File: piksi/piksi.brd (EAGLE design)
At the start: 53 x 53 mm, 157 parts, among them J1 SMA_EDGE, J6 ZX62-B-5PA, Q1 IRLML6401, U1 6SLX9FTG256, U10 MAX2769, U12 PT7M8206B33TA5EX, U13 M25PX80, U2 LTC3407A_DFN, U3 STM32-M-64-LQFP, U4 7Q-16.368MBG-T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

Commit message: Fixed errors eagle 6.5 was complaining about
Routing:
- net SPI2MISO: track 53.6 -> 52.7 mm
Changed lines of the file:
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@@
 <?xml version="1.0" encoding="utf-8"?>
 <!DOCTYPE eagle SYSTEM "eagle.dtd">
-<eagle version="6.2">
+<eagle version="6.5.0">
 <drawing>
 <settings>
@@
 <wire x1="32.1564" y1="48.9204" x2="33.6804" y2="48.9204" width="0.2032" layer="113"/>
 <wire x1="30.861" y1="43.6626" x2="35.5854" y2="43.6626" width="0.2032" layer="113"/>
-<dimension x1="7.4" y1="7.4" x2="7.4" y2="52.4" x3="-0.2" y3="29.9" layer="48"/>
-<dimension x1="7.4" y1="52.4" x2="52.4" y2="52.4" x3="29.9" y3="59.8" layer="48"/>
-<dimension x1="7.9" y1="51.9" x2="4.38175" y2="54.70569375" x3="-1.71655" y3="59.568896875" layer="48" dtype="radius"/>
-<dimension x1="3.4" y1="7.9" x2="56.4" y2="7.9" x3="29.9" y3="-2.4" layer="48"/>
-<dimension x1="7.9" y1="56.4" x2="7.9" y2="3.4" x3="-8.1" y3="29.9" layer="48"/>
-<dimension x1="52.4" y1="7.4" x2="56.4" y2="7.4" x3="54.4" y3="-5.2" layer="48"/>
-<dimension x1="52.4" y1="7.4" x2="52.4" y2="3.4" x3="65.2" y3="5.4" layer="48"/>
-<dimension x1="52.4" y1="52.4" x2="58.8" y2="56.3" x3="61.2" y3="56.3" layer="48" dtype="leader"/>
+<dimension x1="7.4" y1="7.4" x2="7.4" y2="52.4" x3="-0.2" y3="29.9" textsize="3.5" layer="48"/>
+<dimension x1="7.4" y1="52.4" x2="52.4" y2="52.4" x3="29.9" y3="59.8" textsize="3.5" layer="48"/>
+<dimension x1="7.9" y1="51.9" x2="4.38175" y2="54.70569375" x3="-1.71655" y3="59.568896875" textsize="3.5" layer="48" dtype="radius"/>
+<dimension x1="3.4" y1="7.9" x2="56.4" y2="7.9" x3="29.9" y3="-2.4" textsize="3.5" layer="48"/>
+<dimension x1="7.9" y1="56.4" x2="7.9" y2="3.4" x3="-8.1" y3="29.9" textsize="3.5" layer="48"/>
+<dimension x1="52.4" y1="7.4" x2="56.4" y2="7.4" x3="54.4" y3="-5.2" textsize="3.5" layer="48"/>
+<dimension x1="52.4" y1="7.4" x2="52.4" y2="3.4" x3="65.2" y3="5.4" textsize="3.5" layer="48"/>
+<dimension x1="52.4" y1="52.4" x2="58.8" y2="56.3" x3="61.2" y3="56.3" textsize="3.5" layer="48" dtype="leader"/>
 <text x="59" y="57" size="1.778" layer="48">3.5mm dia for M3 loose fit</text>
 <text x="46.7868" y="45.847" size="1.27" layer="122" font="vector" ratio="15" rot="MR0">V+ max 5.5V</text>
@@
 </class>
 </classes>
-<designrules>
+<designrules name="default">
 <description language="de">&lt;b&gt;EAGLE Design Rules&lt;/b&gt;
 &lt;p&gt;
@@
 <signal name="SPI2MISO">
 <contactref element="U1" pad="P10"/>
-<contactref element="U13" pad="2"/>
 <contactref element="U3" pad="35"/>
 <wire x1="38.6134" y1="32.6924" x2="38.6134" y2="35.2752" width="0.1778" layer="1"/>
@@
 <wire x1="35.1798" y1="45.8978" x2="35.55" y2="46.268" width="0.1524" layer="15"/>
 <wire x1="35.55" y1="46.268" x2="35.7464" y2="46.268" width="0.254" layer="1"/>
-<wire x1="35.7464" y1="46.268" x2="36.3756" y2="45.6388" width="0.254" layer="1"/>
 <wire x1="28.321" y1="44.7802" x2="26.1874" y2="44.7802" width="0.1524" layer="15"/>
 <wire x1="26.1874" y1="44.7802" x2="25.1714" y2="43.7642" width="0.1524" layer="15"/>
@@
 <wire x1="13.462" y1="36.449" x2="13.462" y2="40.0304" width="0.1524" layer="15"/>
 <wire x1="13.462" y1="40.0304" x2="13.5128" y2="40.0812" width="0.1524" layer="15"/>
+<contactref element="U13" pad="2"/>
+<wire x1="35.7464" y1="46.268" x2="36.3756" y2="45.6388" width="0" layer="19" extent="1-1"/>
 </signal>
 <signal name="N$34">
@@
 </signal>
 <signal name="SPI2NSS_FLASH">
-<contactref element="U1" pad="T3"/>
 <contactref element="R13" pad="P$1"/>
 <contactref element="U13" pad="1"/>
@@
 <wire x1="36.4722" y1="44.45" x2="36.3756" y2="44.3788" width="0.1778" layer="1"/>
 <via x="35.5346" y="45.0134" extent="1-16" drill="0.3"/>
-<wire x1="13.566" y1="44.3572" x2="13.566" y2="44.3762" width="0.1524" layer="1"/>
 <wire x1="13.566" y1="44.3762" x2="13.0683" y2="43.8277" width="0.1524" layer="1"/>
 <via x="13.0683" y="43.8277" extent="1-16" drill="0.3"/>
@@
 <wire x1="15.3416" y1="43.2054" x2="13.6906" y2="43.2054" width="0.1524" layer="15"/>
 <wire x1="13.6906" y1="43.2054" x2="13.0683" y2="43.8277" width="0.1524" layer="15"/>
+<contactref element="U1" pad="T3"/>
+<wire x1="13.566" y1="44.3572" x2="13.566" y2="44.3762" width="0" layer="19" extent="1-1"/>
 </signal>
 <signal name="N$11">
@@
 <signal name="SPI2SCK">
 <contactref element="U1" pad="R11"/>
-<contactref element="U13" pad="6"/>
 <contactref element="U3" pad="34"/>
 <wire x1="37.6428" y1="17.0942" x2="37.6428" y2="16.1544" width="0.1524" layer="1"/>
@@
 <wire x1="43.6245" y1="18.7833" x2="40.9956" y2="16.1544" width="0.1524" layer="15"/>
 <wire x1="40.9956" y1="16.1544" x2="37.6428" y2="16.1544" width="0.1524" layer="15"/>
-<wire x1="30.3756" y1="46.9188" x2="30.6429625" y2="46.9188" width="0.254" layer="1"/>
 <wire x1="30.6429625" y1="46.9188" x2="31.22168125" y2="46.34008125" width="0.254" layer="1"/>
 <wire x1="40.592" y1="20.8624" x2="40.592" y2="20.0434" width="0.1524" layer="1"/>
@@
 <wire x1="45.6184" y1="27.0256" x2="49.1744" y2="27.0256" width="0.1524" layer="15"/>
 <wire x1="49.1744" y1="27.0256" x2="50.1396" y2="26.0604" width="0.1524" layer="15"/>
+<contactref element="U13" pad="6"/>
+<wire x1="30.6429625" y1="46.9188" x2="30.3756" y2="46.9188" width="0" layer="19" extent="1-1"/>
 </signal>
 <signal name="SPI2NSS_MAX">
@@
 <signal name="SPI2MOSI">
 <contactref element="U1" pad="T10"/>
-<contactref element="U13" pad="5"/>
 <contactref element="U3" pad="36"/>
 <via x="36.3982" y="16.3576" extent="1-16" drill="0.3"/>
@@
 <wire x1="31.21151875" y1="47.5796" x2="31.21151875" y2="47.13731875" width="0.1524" layer="15"/>
 <wire x1="31.21151875" y1="47.13731875" x2="28.4988" y2="44.4246" width="0.1524" layer="15"/>
-<wire x1="30.3756" y1="48.1788" x2="30.61231875" y2="48.1788" width="0.254" layer="1"/>
 <wire x1="30.61231875" y1="48.1788" x2="31.21151875" y2="47.5796" width="0.254" layer="1"/>
 <wire x1="40.092" y1="20.8624" x2="40.092" y2="20.0514" width="0.1524" layer="1"/>
@@
 <wire x1="46.4058" y1="27.3304" x2="44.8056" y2="28.9306" width="0.1524" layer="15"/>
 <wire x1="20.4978" y1="42.3164" x2="21.2852" y2="42.3164" width="0.1524" layer="15"/>
+<contactref element="U13" pad="5"/>
+<wire x1="30.61231875" y1="48.1788" x2="30.3756" y2="48.1788" width="0" layer="19" extent="1-1"/>
 </signal>
 <signal name="DEBUG6">

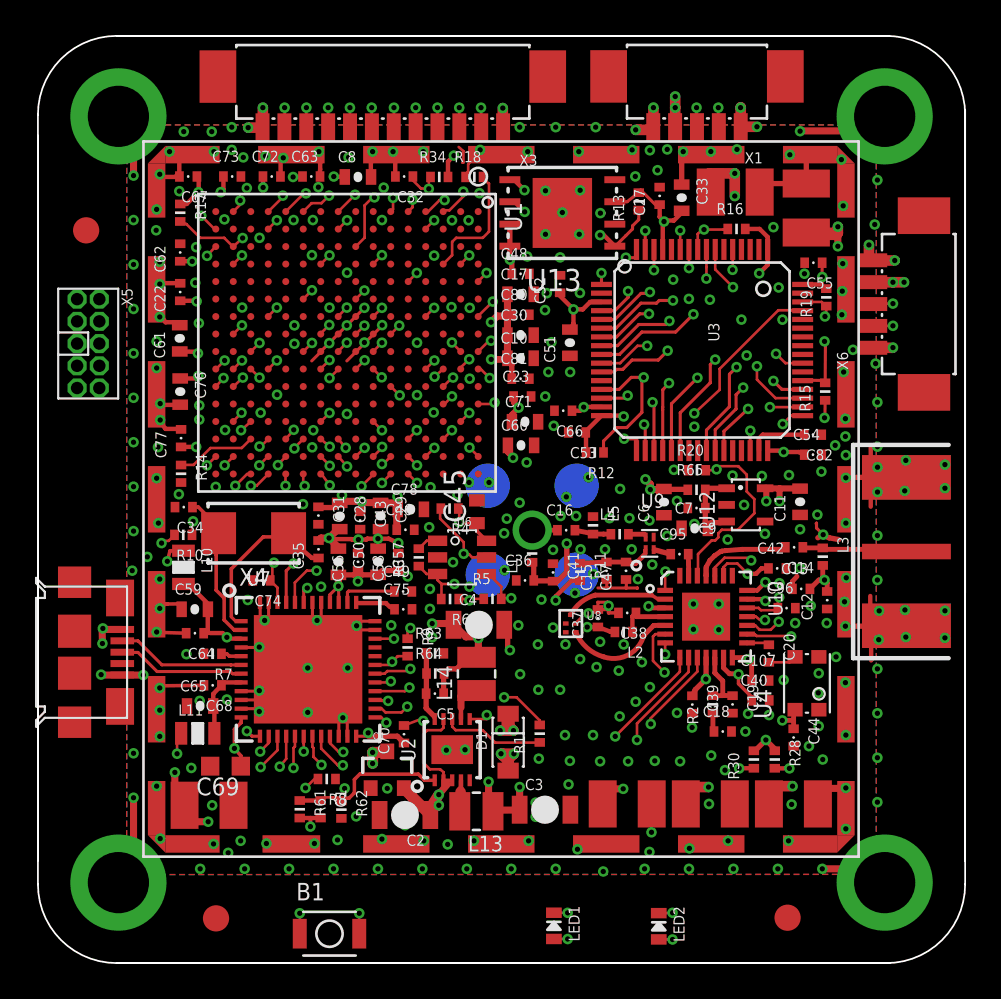
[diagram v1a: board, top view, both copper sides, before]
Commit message: Snapped all elements on schematic to 0.1 inch grid
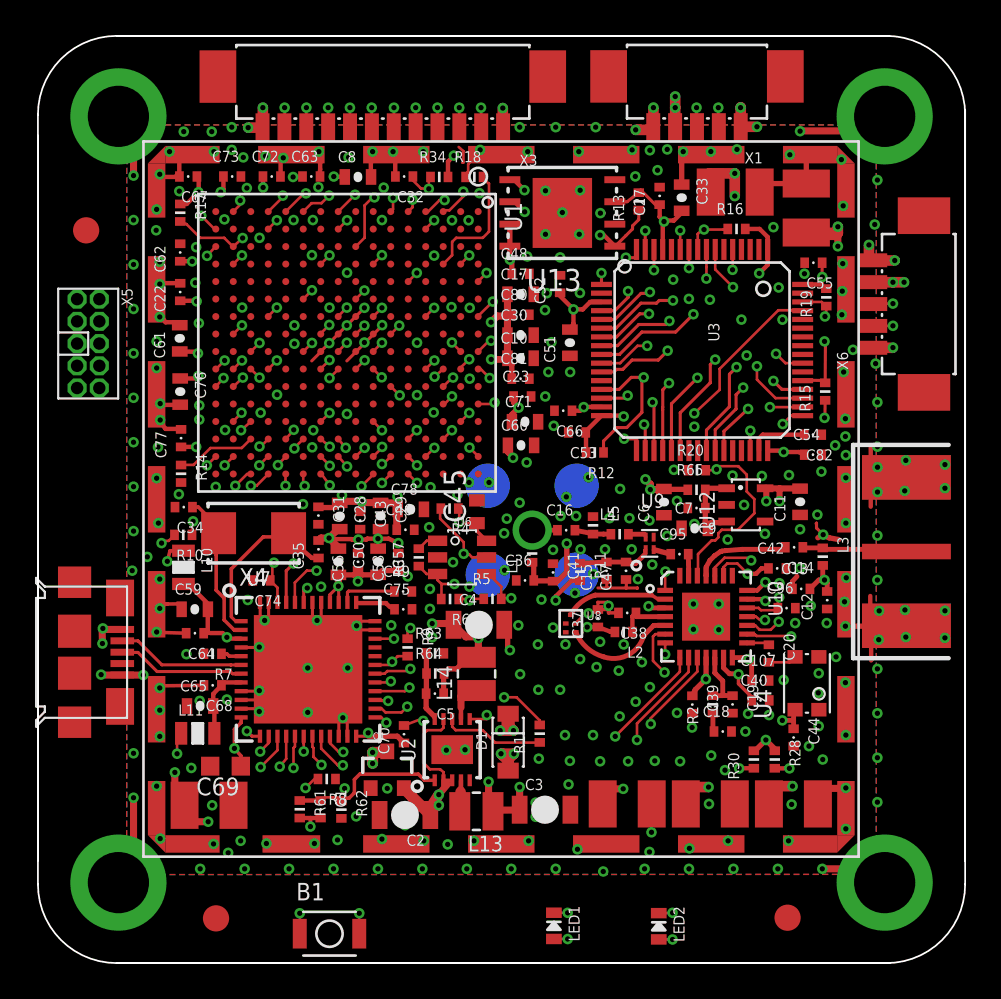
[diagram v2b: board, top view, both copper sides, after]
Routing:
- net GND: track 153.2 -> 150.4 mm
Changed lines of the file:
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@@
 <contactref element="J6" pad="PIN_5"/>
 <contactref element="SHLD2" pad="21"/>
-<contactref element="SHLD2" pad="1"/>
-<contactref element="SHLD2" pad="28"/>
-<contactref element="SHLD2" pad="27"/>
-<contactref element="SHLD2" pad="26"/>
-<contactref element="SHLD2" pad="25"/>
-<contactref element="SHLD2" pad="24"/>
-<contactref element="SHLD2" pad="23"/>
-<contactref element="SHLD2" pad="22"/>
 <contactref element="SHLD2" pad="20"/>
 <contactref element="SHLD2" pad="19"/>
@@
 <contactref element="SHLD2" pad="8"/>
 <contactref element="SHLD2" pad="7"/>
-<contactref element="SHLD2" pad="6"/>
-<contactref element="SHLD2" pad="5"/>
-<contactref element="SHLD2" pad="4"/>
-<contactref element="SHLD2" pad="3"/>
-<contactref element="SHLD2" pad="2"/>
 <contactref element="U3" pad="12"/>
 <contactref element="U3" pad="60"/>
@@
 <wire x1="11.4808" y1="49.2252" x2="11.4808" y2="48.4482" width="0.254" layer="1"/>
 <wire x1="11.4808" y1="48.4482" x2="11.4888" y2="48.3616" width="0.254" layer="1"/>
-<wire x1="10.186" y1="47.56" x2="10.186" y2="48.1336" width="0.254" layer="1"/>
 <wire x1="10.186" y1="48.1336" x2="10.5664" y2="48.3362" width="0.254" layer="1"/>
 <wire x1="10.5664" y1="48.3362" x2="11.4046" y2="48.3362" width="0.254" layer="1"/>
@@
 <wire x1="49.5554" y1="22.6568" x2="50.9778" y2="22.6568" width="0.3048" layer="1"/>
 <wire x1="50.9778" y1="22.6568" x2="51.0286" y2="23.114" width="0.3048" layer="1"/>
-<wire x1="49.586" y1="29.91" x2="49.586" y2="30.1042" width="0.3048" layer="1"/>
-<wire x1="49.586" y1="30.1042" x2="49.784" y2="31.1658" width="0.3048" layer="1"/>
-<wire x1="49.784" y1="31.1658" x2="50.6984" y2="31.1658" width="0.3048" layer="1"/>
-<wire x1="50.6984" y1="31.1658" x2="50.7492" y2="31.1912" width="0.3048" layer="1"/>
 <via x="52.959" y="23.5854" extent="1-16" drill="0.3"/>
 <via x="51.4858" y="23.5354" extent="1-16" drill="0.3"/>
@@
 <wire x1="34.1457" y1="22.8427" x2="34.4932" y2="23.1902" width="0.1524" layer="1"/>
 <via x="34.0968" y="24.5526" extent="1-16" drill="0.3"/>
+<contactref element="SHLD2" pad="22"/>
+<contactref element="SHLD2" pad="23"/>
+<contactref element="SHLD2" pad="24"/>
+<contactref element="SHLD2" pad="25"/>
+<contactref element="SHLD2" pad="26"/>
+<contactref element="SHLD2" pad="27"/>
+<contactref element="SHLD2" pad="28"/>
+<contactref element="SHLD2" pad="6"/>
+<contactref element="SHLD2" pad="5"/>
+<contactref element="SHLD2" pad="4"/>
+<contactref element="SHLD2" pad="3"/>
+<contactref element="SHLD2" pad="2"/>
+<contactref element="SHLD2" pad="1"/>
+<wire x1="53.045359375" y1="31.1658" x2="53.045359375" y2="31.1658" width="0" layer="19" extent="1-16"/>
 </signal>
 <signal name="N$3">

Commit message: Board with new logo and updated library
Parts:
- moved U$2 1.88 mm to (27.9, 2.90)
